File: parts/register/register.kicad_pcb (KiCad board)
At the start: 4 copper layers, 100.8 x 40 mm, 33 parts, among them J1 BUS, J2 CLR, J3 CLK, J4 ~{RI}, J5 ~RO, J6 DATA, J7 CONN_PWR, U1 74HC245, U2 74HC173, U3 74HC173

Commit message: SMD Register
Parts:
- removed C11: 0.1µF, Capacitor_SMD:C_0805_2012Metric
- removed D10, D11, D12, D13, D14, D15, D16, D17: RED, LED_THT:LED_D5.0mm
- removed J2: CLR, Connector_PinHeader_2.54mm:PinHeader_1x01_P2.54mm_Vertical
- removed J3: CLK, Connector_PinHeader_2.54mm:PinHeader_1x01_P2.54mm_Vertical
- removed J4: ~{RI}, Connector_PinHeader_2.54mm:PinHeader_1x01_P2.54mm_Vertical
- removed J5: ~RO, Connector_PinHeader_2.54mm:PinHeader_1x01_P2.54mm_Vertical
- removed J6: DATA, Connector_PinHeader_2.54mm:PinHeader_1x08_P2.54mm_Vertical
- removed J7: CONN_PWR, Connector_PinHeader_2.54mm:PinHeader_1x02_P2.54mm_Vertical
- removed R24, R25, R26, R27, R28, R29, R30, R31: 220, Resistor_SMD:R_0805_2012Metric
- added C3: 0.1µF, Capacitor_SMD:C_0805_2012Metric, F.Cu at (124.5, 63.5)
- added D1: RED, LED_SMD:LED_0805_2012Metric, F.Cu at (189.2, 65.3)
- added D2: RED, LED_SMD:LED_0805_2012Metric, F.Cu at (183.2, 68.4)
- added D3: RED, LED_SMD:LED_0805_2012Metric, F.Cu at (178.8, 68.4)
- added D4: RED, LED_SMD:LED_0805_2012Metric, F.Cu at (193.7, 61.9)
- added D5: RED, LED_SMD:LED_0805_2012Metric, F.Cu at (184.8, 62.3)
- added D6: RED, LED_SMD:LED_0805_2012Metric, F.Cu at (183.2, 65.4)
- added D7: RED, LED_SMD:LED_0805_2012Metric, F.Cu at (193.7, 64.9)
- added D8: RED, LED_SMD:LED_0805_2012Metric, F.Cu at (198.1, 61.9)
- added R1: 220, Resistor_SMD:R_0805_2012Metric, F.Cu at (178.8, 74.3)
- added R2: 220, Resistor_SMD:R_0805_2012Metric, F.Cu at (183.2, 74.3)
- added R3: 220, Resistor_SMD:R_0805_2012Metric, F.Cu at (183.2, 71.4)
- added R4: 220, Resistor_SMD:R_0805_2012Metric, F.Cu at (178.8, 77.3)
- added R5: 220, Resistor_SMD:R_0805_2012Metric, F.Cu at (178.8, 71.4)
- added R6: 220, Resistor_SMD:R_0805_2012Metric, F.Cu at (187.7, 68.3)
- added R7: 220, Resistor_SMD:R_0805_2012Metric, F.Cu at (187.7, 71.3)
- added R8: 220, Resistor_SMD:R_0805_2012Metric, F.Cu at (192.1, 68.3)
- H1: value MountingHole1 -> MountingHole4; footprint MountingHole:MountingHole_2.2mm_M2_DIN965_Pad -> MountingHole:MountingHole_2.2mm_M2_Pad_Via
- H2: value MountingHole2 -> MountingHole3; footprint MountingHole:MountingHole_2.2mm_M2_DIN965_Pad -> MountingHole:MountingHole_2.2mm_M2_Pad_Via
- H3: value MountingHole3 -> MountingHole2; footprint MountingHole:MountingHole_2.2mm_M2_DIN965_Pad -> MountingHole:MountingHole_2.2mm_M2_Pad_Via
- H4: value MountingHole4 -> MountingHole1; footprint MountingHole:MountingHole_2.2mm_M2_DIN965_Pad -> MountingHole:MountingHole_2.2mm_M2_Pad_Via
- J1: value BUS -> Conn_02x12_Odd_Even; footprint Connector_PinHeader_2.54mm:PinHeader_1x08_P2.54mm_Vertical -> Connector_IDC:IDC-Header_2x12_P2.54mm_Vertical; moved to F.Cu
- U1: footprint Package_DIP:DIP-20_W7.62mm -> Package_SO:TSSOP-20_4.4x6.5mm_P0.65mm
- U2, U3: footprint Package_DIP:DIP-16_W7.62mm -> Package_SO:SOIC-16_3.9x9.9mm_P1.27mm
- moved H2 112.8 mm to (68.6, 91.4)
- moved H4 98.9 mm to (144.8, 91.4)
- moved U3 46.8 mm to (132.1, 66.0)
- moved U1 44.2 mm to (96.5, 66.0)
- moved J1 39.0 mm to (76.2, 53.3), turned to 0 degrees
- moved C1 36.6 mm to (91.4, 63.5), turned to -90 degrees
- moved C2 35.2 mm to (106.7, 63.5), turned to -90 degrees
- moved U2 32.2 mm to (114.3, 66.0)
- moved H1 31.6 mm to (68.6, 43.2)
- moved H3 8.87 mm to (144.8, 43.2)
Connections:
- J1 pad 1: Net-(J1-Pad1) -> GND
- J1 pad 2: Net-(J1-Pad2) -> VCC
- J1 pad 3: Net-(J1-Pad3) -> GND
- J1 pad 4: Net-(J1-Pad4) -> VCC
- J1 pad 5: Net-(J1-Pad5) -> ~{RI}
- J1 pad 6: Net-(J1-Pad6) -> CLK
- J1 pad 7: Net-(J1-Pad7) -> ~{RO}
- J1 pad 8: Net-(J1-Pad8) -> CLR
- U1 pad 11: Net-(J1-Pad1) -> /BUS7
- U1 pad 12: Net-(J1-Pad2) -> /BUS6
- U1 pad 13: Net-(J1-Pad3) -> /BUS5
- U1 pad 14: Net-(J1-Pad4) -> /BUS4
- U1 pad 15: Net-(J1-Pad5) -> /BUS3
- U1 pad 16: Net-(J1-Pad6) -> /BUS2
- U1 pad 17: Net-(J1-Pad7) -> /BUS1
- U1 pad 18: Net-(J1-Pad8) -> /BUS0
- U1 pad 19: /~{RO} -> ~{RO}
- U1 pad 2: Net-(D10-Pad2) -> /DATA0
- U1 pad 3: Net-(D11-Pad2) -> /DATA1
- U1 pad 4: Net-(D12-Pad2) -> /DATA2
- U1 pad 5: Net-(D13-Pad2) -> /DATA3
- U1 pad 6: Net-(D14-Pad2) -> /DATA4
- U1 pad 7: Net-(D15-Pad2) -> /DATA5
- U1 pad 8: Net-(D16-Pad2) -> /DATA6
- U1 pad 9: Net-(D17-Pad2) -> /DATA7
- U2 pad 10: /~{RI} -> ~{RI}
- U2 pad 11: Net-(J1-Pad5) -> /BUS0
- U2 pad 12: Net-(J1-Pad6) -> /BUS1
- U2 pad 13: Net-(J1-Pad7) -> /BUS2
- U2 pad 14: Net-(J1-Pad8) -> /BUS3
- U2 pad 15: /CLR -> CLR
- U2 pad 3: Net-(D10-Pad2) -> /DATA3
- U2 pad 4: Net-(D11-Pad2) -> /DATA2
- U2 pad 5: Net-(D12-Pad2) -> /DATA1
- U2 pad 6: Net-(D13-Pad2) -> /DATA0
- U2 pad 7: /CLK -> CLK
- U2 pad 9: /~{RI} -> ~{RI}
- U3 pad 10: /~{RI} -> ~{RI}
- U3 pad 11: Net-(J1-Pad1) -> /BUS4
- U3 pad 12: Net-(J1-Pad2) -> /BUS5
- U3 pad 13: Net-(J1-Pad3) -> /BUS6
- U3 pad 14: Net-(J1-Pad4) -> /BUS7
- U3 pad 15: /CLR -> CLR
- U3 pad 3: Net-(D14-Pad2) -> /DATA7
- U3 pad 4: Net-(D15-Pad2) -> /DATA6
- U3 pad 5: Net-(D16-Pad2) -> /DATA5
- U3 pad 6: Net-(D17-Pad2) -> /DATA4
- U3 pad 7: /CLK -> CLK
- U3 pad 9: /~{RI} -> ~{RI}
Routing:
- net GND: track 16.6 -> 389.1 mm, vias 11 -> 0
- net Net-(D10-Pad2): track 172.9 -> 0.00 mm
- net Net-(D11-Pad2): track 159.9 -> 0.00 mm
- net Net-(D12-Pad2): track 152.1 -> 0.00 mm
- net Net-(D13-Pad2): track 141.9 -> 0.00 mm
- net Net-(D17-Pad2): track 128.4 -> 0.00 mm
- net Net-(D16-Pad2): track 121.5 -> 0.00 mm
- net Net-(D15-Pad2): track 114.7 -> 0.00 mm
- net Net-(D14-Pad2): track 110.7 -> 0.00 mm
- net Net-(J1-Pad5): track 102.1 -> 0.00 mm
- net Net-(J1-Pad6): track 101.3 -> 0.00 mm
- net Net-(J1-Pad7): track 100.9 -> 0.00 mm
- net Net-(J1-Pad8): track 99.8 -> 0.00 mm
- net /DATA7: track 0.00 -> 89.9 mm, vias 0 -> 2
- net /DATA5: track 0.00 -> 88.1 mm, vias 0 -> 4
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- added copper zone on F.Cu, net GND
- added copper zone on In2.Cu, net VCC
- removed copper zone on In2.Cu, net GND
- removed copper zone on F.Cu, net VCC
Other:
- board size 100.8 x 40 mm -> 81.3 x 53.3 mm
- board text removed: "BUS_0"
- board text removed: "BUS_1"
- board text removed: "BUS_2"
- board text removed: "BUS_3"
- board text removed: "BUS_4"
- board text removed: "BUS_5"
- board text removed: "BUS_6"
- board text removed: "BUS_7"
- board text removed: "GND"
- board text removed: "REG_0"
- board text removed: "REG_1"
- board text removed: "REG_2"
- board text removed: "REG_3"
- board text removed: "REG_4"
- board text removed: "REG_5"
- board text removed: "REG_6"
- board text removed: "REG_7"
- board text removed: "VCC"

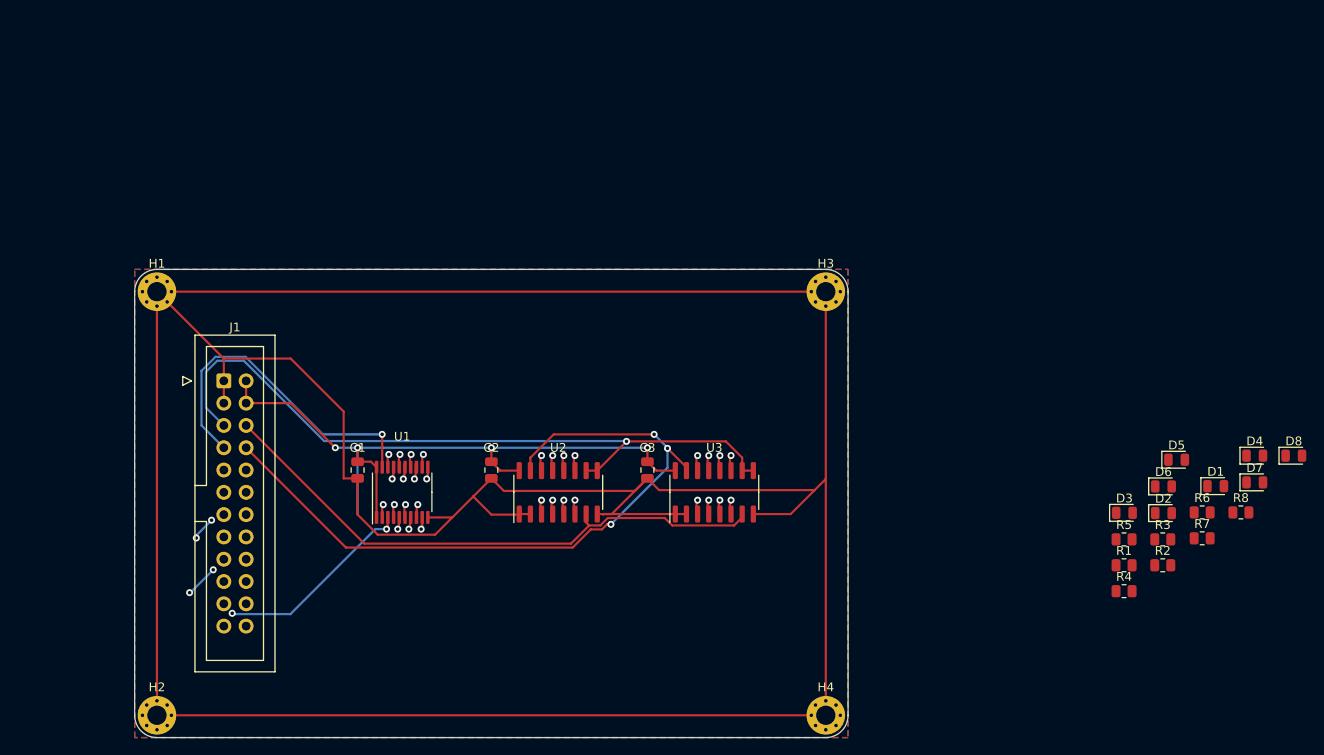
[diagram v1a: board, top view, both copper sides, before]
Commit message: Create PCB for Register
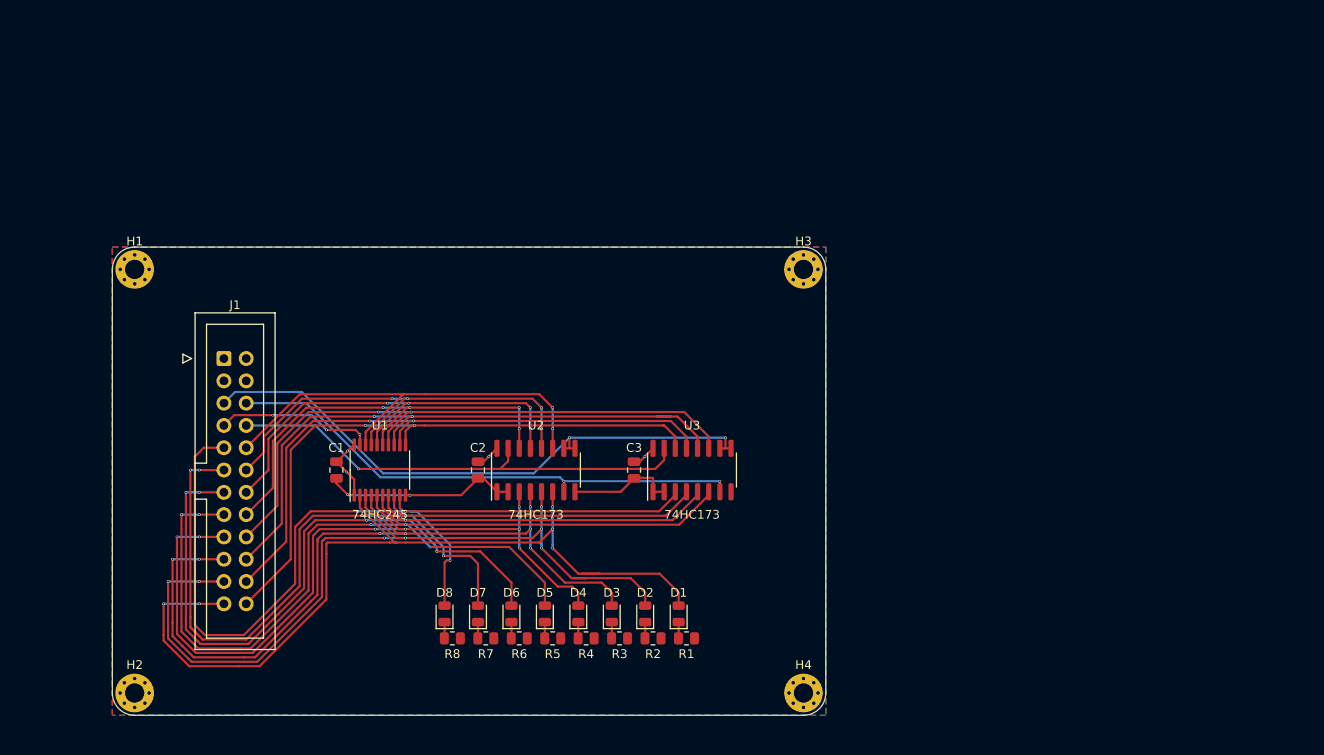
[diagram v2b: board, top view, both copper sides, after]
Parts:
- moved D8 98.4 mm to (101.3, 79.9), turned to 90 degrees
- moved R8 91.0 mm to (102.2, 82.7)
- moved D7 89.8 mm to (105.2, 79.9), turned to 90 degrees
- moved R7 82.4 mm to (106.0, 82.7)
- moved D4 79.1 mm to (116.6, 79.9), turned to 90 degrees
- moved R6 79.1 mm to (109.9, 82.7)
- moved D6 75.7 mm to (109.0, 79.9), turned to 90 degrees
- moved D5 74.1 mm to (112.8, 79.9), turned to 90 degrees
- moved R5 66.1 mm to (113.7, 82.7)
- moved R3 62.9 mm to (121.3, 82.7)
- moved D1 62.9 mm to (128.0, 79.9), turned to 90 degrees
- moved R4 61.5 mm to (117.5, 82.7)
- moved D2 60.1 mm to (124.2, 79.9), turned to 90 degrees
- moved D3 59.5 mm to (120.4, 79.9), turned to 90 degrees
- moved R2 58.7 mm to (125.1, 82.7)
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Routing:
- net GND: track 389.1 -> 35.0 mm, vias 0 -> 2
- net VCC: track 78.1 -> 13.1 mm
- net /DATA0: track 52.2 -> 100.6 mm, vias 2 -> 5
- net /BUS5: track 27.7 -> 71.6 mm
- net /BUS4: track 27.6 -> 70.3 mm
- net /BUS7: track 30.9 -> 69.3 mm
- net /BUS6: track 31.7 -> 69.6 mm
- net /DATA1: track 60.0 -> 97.6 mm, vias 3 -> 7
- net /DATA2: track 57.0 -> 92.4 mm, vias 2 -> 7
- net /DATA4: track 83.8 -> 117.0 mm, vias 2 -> 5
- net /BUS1: track 20.8 -> 50.7 mm, vias 2 -> 4
- net /BUS0: track 20.3 -> 50.3 mm
- net CLR: track 81.0 -> 54.1 mm, vias 3 -> 1
- net /DATA3: track 62.5 -> 88.8 mm, vias 4 -> 7
- net /BUS2: track 23.9 -> 50.0 mm, vias 2 -> 4
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- added copper zone on B.Cu, net VCC
- removed copper zone on B.Cu, net GND
- removed copper zone on In1.Cu, net VCC
- removed copper zone on In2.Cu, net VCC
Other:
- copper layers 4 -> 2

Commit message: SMD Clock
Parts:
- moved U2 18.8 mm to (130.6, 63.4)
- moved U3 16.8 mm to (112.8, 63.4)
- moved U1 1.40 mm to (95.4, 63.4)
- moved C1 1.15 mm to (90.2, 63.4)
- moved C2 0.77 mm to (105.9, 63.4)
- moved C3 0.77 mm to (123.7, 63.4)
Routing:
- net GND: track 35.0 -> 547.1 mm
- net VCC: track 13.1 -> 51.5 mm, vias 4 -> 8
- net /DATA4: track 117.0 -> 84.9 mm, vias 5 -> 4
- net /DATA5: track 112.5 -> 85.0 mm, vias 5 -> 4
- net CLK: track 60.1 -> 83.3 mm
- net /BUS0: track 50.3 -> 73.1 mm, vias 2 -> 0
- net /DATA6: track 110.7 -> 88.4 mm, vias 5 -> 4
- net /BUS2: track 50.0 -> 71.7 mm, vias 4 -> 2
- net /BUS1: track 50.7 -> 72.4 mm, vias 4 -> 2
- net /BUS3: track 49.7 -> 71.0 mm, vias 4 -> 2
- net /DATA0: track 100.6 -> 83.3 mm, vias 5 -> 0
- net /BUS5: track 71.6 -> 56.1 mm
- net /DATA7: track 106.4 -> 91.7 mm, vias 3 -> 4
- net /BUS7: track 69.3 -> 54.7 mm
- net /BUS6: track 69.6 -> 55.4 mm
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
